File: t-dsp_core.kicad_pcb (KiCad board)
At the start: 4 copper layers, 100 x 61 mm, 160 parts, among them IC1 Logic Level Shifter - 74HCT2G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, J1 J_PWR, J10 J_DMX, J11 J_LED, J12 J_ETH, J13 u.FL DNP (IDC767 ext-antenna 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, J2 J_TDM, J3 J_T, J4 J_USBH, J5 J_MIDI, J6 J_SPDIF, J7 J_AUX, J8 J_S3, T108 Tab, T109 Tab, T110 Tab, T111 Tab, U1 Teensy 4.1 - DEVKIT, U11 Dual Buffer - SN74LVC2G125DCTR, U13 ESP32-S3-WROOM-1-N16R8, U15 LT3045EMSE#TRPBF, U16 THVD1450DR, U17 ISO7762DW, U18 TEA1-0505HI, U19 SRC4382IPFBR, U20 TLV75718PDRVR, U21 74LVC157APW, U22 IDC777-1, U23 74LVC157APW, U24 AP63203WU, U3 Power Mux & Protect - TPS2116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, U4 Optoisolators - H11L1SM - 6-S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, U5 SN74LVC541APWR, U9 Dual Buffer - 74HCT2G17GW,125, Y1 24.576MHz

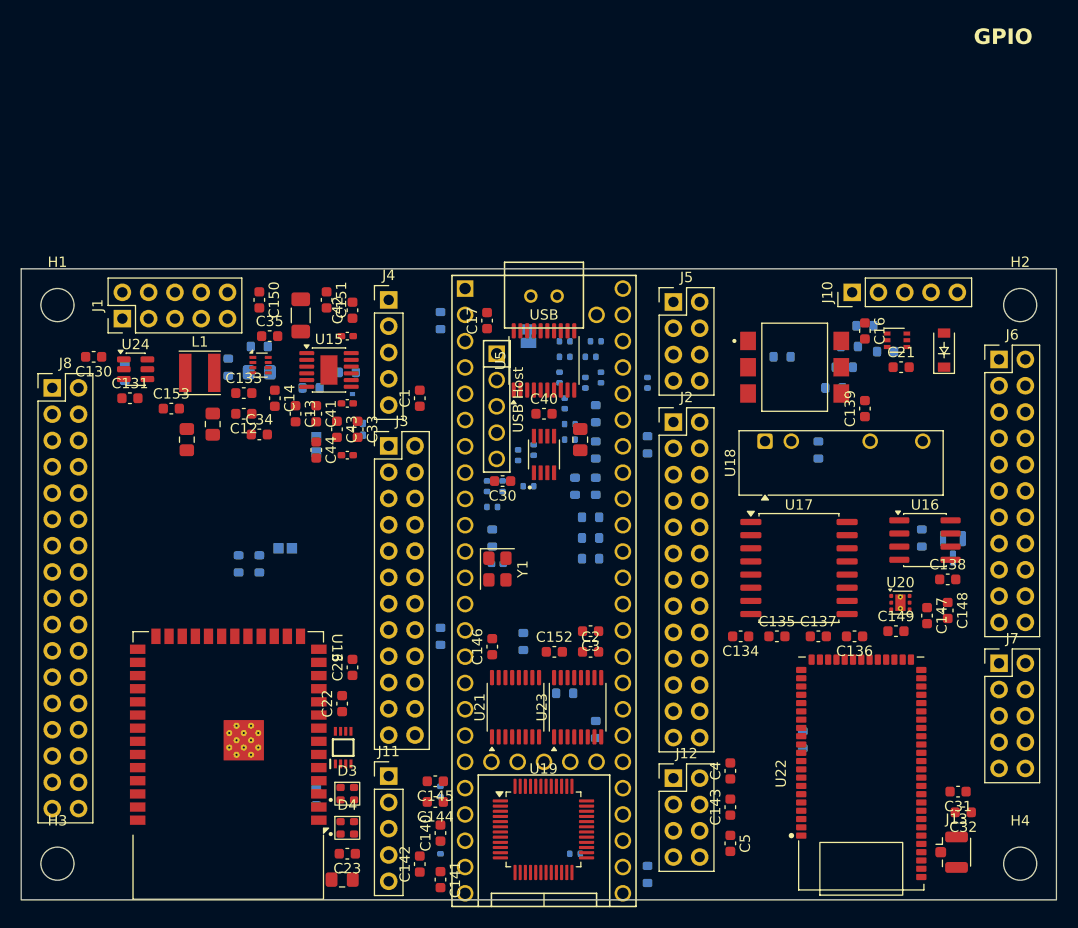
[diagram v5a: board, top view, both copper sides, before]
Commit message: Spin 2 stage 10v (board): J2 2x14, U6/U7 in the buffer column under the Teensy, 3 series R + 8 jumpers + 2 caps added and placed (back side), two stray track fragments from the old design removed; synced with pcbnew, parity clean
Co-Authored-By: Claude Fable 5.1 <noreply@anthropic.com>
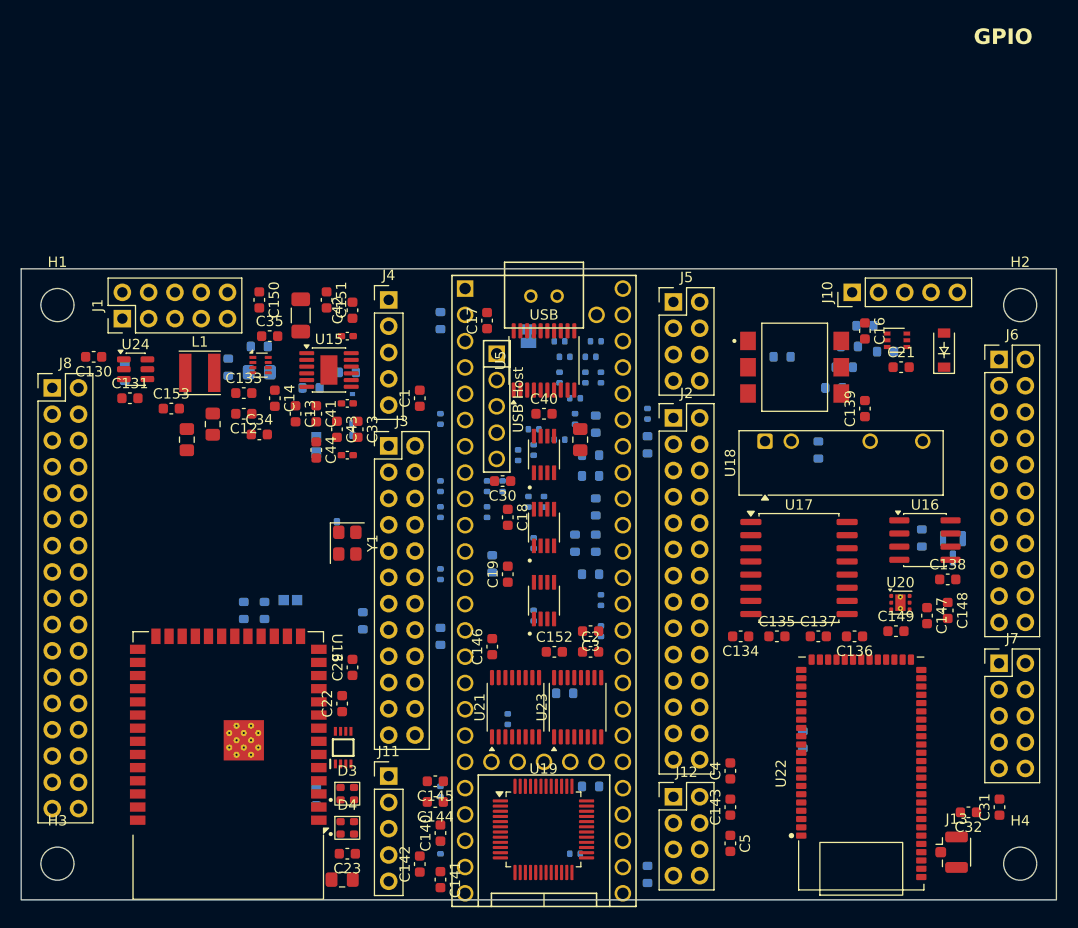
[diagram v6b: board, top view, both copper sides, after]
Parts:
- added C18: 100nF, Capacitor_SMD:C_0603_1608Metric, F.Cu at (147.0, 163.0)
- added C19: 100nF, Capacitor_SMD:C_0603_1608Metric, F.Cu at (147.0, 168.5)
- added R75: 33 ohm, Resistor_SMD:R_0402_1005Metric, B.Cu at (156.0, 174.0)
- added R76: 33 ohm, Resistor_SMD:R_0402_1005Metric, B.Cu at (147.0, 182.5)
- added R77: 0 ohm, Resistor_SMD:R_0402_1005Metric, B.Cu at (149.5, 165.5)
- added R78: 0 ohm DNP, Resistor_SMD:R_0402_1005Metric, B.Cu at (140.5, 162.5)
- added R79: 0 ohm DNP, Resistor_SMD:R_0402_1005Metric, B.Cu at (149.0, 161.5)
- added R80: 0 ohm, Resistor_SMD:R_0402_1005Metric, B.Cu at (140.5, 160.0)
- added R81: 33 ohm, Resistor_SMD:R_0402_1005Metric, B.Cu at (156.0, 171.0)
- added R82: 0 ohm DNP, Resistor_SMD:R_0402_1005Metric, B.Cu at (149.5, 172.5)
- added R83: 0 ohm, Resistor_SMD:R_0402_1005Metric, B.Cu at (140.5, 168.5)
- added R84: 0 ohm, Resistor_SMD:R_0402_1005Metric, B.Cu at (149.5, 154.5)
- added R85: 0 ohm DNP, Resistor_SMD:R_0402_1005Metric, B.Cu at (140.5, 153.5)
- added U6: SN74LVC2G125DCTR, project_fp:SOP65P400X130-8N, F.Cu at (150.5, 164.0)
- added U7: SN74LVC2G125DCTR, project_fp:SOP65P400X130-8N, F.Cu at (150.5, 171.1)
- J2: footprint Connector_PinHeader_2.54mm:PinHeader_2x13_P2.54mm_Vertical -> Connector_PinHeader_2.54mm:PinHeader_2x14_P2.54mm_Vertical
- moved R60 15.9 mm to (130.5, 164.0), turned to 90 degrees
- moved R61 15.6 mm to (133.0, 173.0)
- moved Y1 14.7 mm to (131.5, 165.5)
- moved R47 7.83 mm to (153.5, 153.5)
- moved R6 7.57 mm to (160.5, 153.0), turned to 90 degrees
- moved R11 5.52 mm to (155.0, 189.0), turned to 0 degrees
- moved R12 5.50 mm to (155.5, 162.0), turned to -90 degrees
- moved PU_EN1 5.02 mm to (126.0, 171.0)
- moved R67 4.53 mm to (123.5, 172.0)
- moved R68 4.53 mm to (121.5, 172.0)
- moved C31 4.27 mm to (194.5, 191.0), turned to 90 degrees
- moved R14 3.35 mm to (155.0, 157.0), turned to 180 degrees
- moved R15 2.55 mm to (155.5, 165.5), turned to 90 degrees
- moved R19 2.50 mm to (145.5, 167.5)
- moved R56 2.12 mm to (150.5, 161.5), turned to -90 degrees
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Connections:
- net Net-(U1-32_OUT1B) renamed /OUT1B_MCU
- U11 pad 7: GND -> /OUT1C_OE_IN

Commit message: Spin 2 stage 10w: LED driver IC1 and D3/D4 to the middle of the left column; passives re-placed
Co-Authored-By: Claude Fable 5.1 <noreply@anthropic.com>
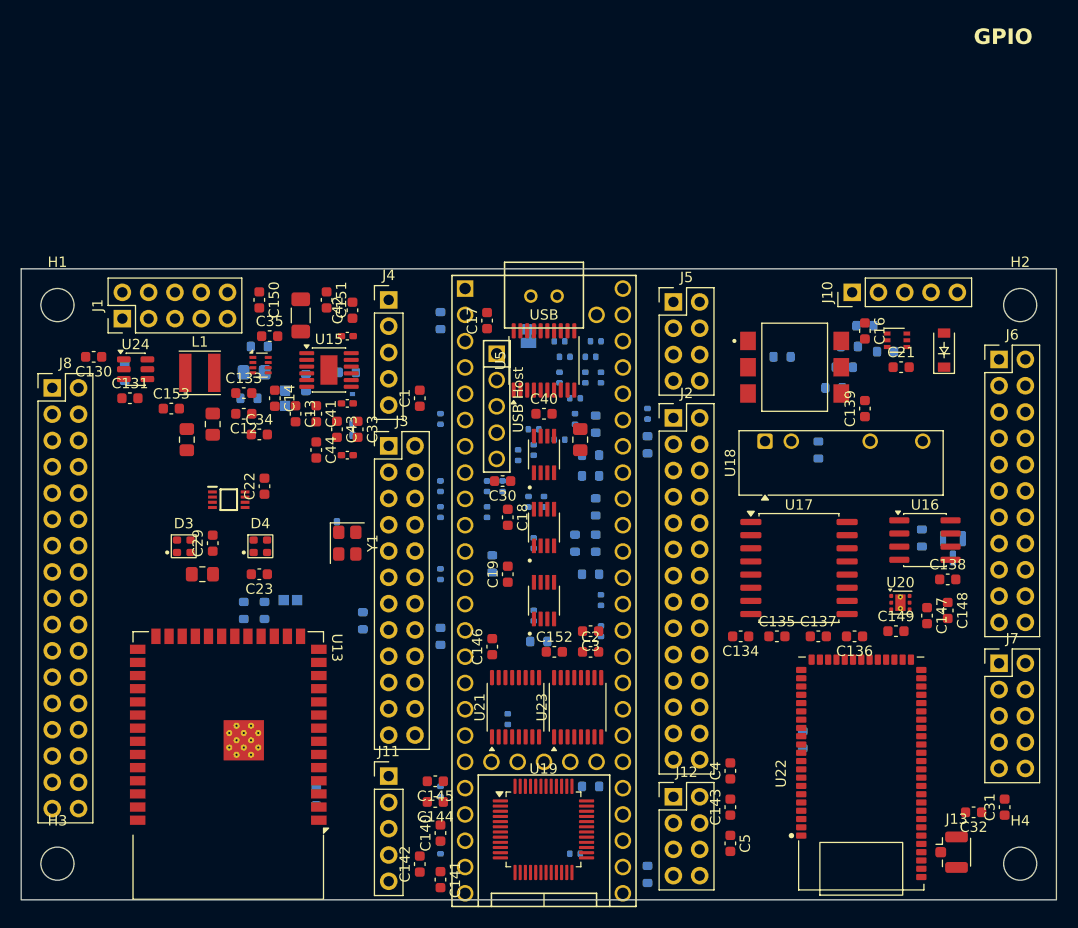
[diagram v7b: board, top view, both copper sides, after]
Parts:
- moved C28 32.4 mm to (117.5, 168.5), turned to 0 degrees
- moved D3 28.7 mm to (115.7, 165.8)
- moved D4 28.5 mm to (123.1, 165.8)
- moved C23 28.3 mm to (123.0, 168.5)
- moved IC1 26.4 mm to (120.0, 161.3), turned to 0 degrees
- moved C22 22.3 mm to (123.5, 160.0)
- moved C29 18.1 mm to (118.5, 165.5)
- moved R8 5.59 mm to (150.0, 175.0)
- moved FL1 5.41 mm to (125.5, 151.5)
- moved R29 3.61 mm to (122.0, 151.5), turned to 0 degrees
- moved R58 0.71 mm to (127.5, 150.0), turned to -90 degrees
- moved C31 0.50 mm to (195.0, 191.0)
- moved C32 0.50 mm to (192.0, 191.5)
- moved R28 0.50 mm to (122.5, 149.0)

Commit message: Spin 2 stage 10y (2/2, board): SAI2 block footprints synced and placed; stage 10x power parts placed
- swap_fp/sync_fields from the stage 10y netlist: U19 TSSOP-16 (257), U21 TSSOP-20 (244), U23 TSSOP-16 (138), U20 SOP-8 (2G125), J7 2x6 J_SAI2, J4 2x5 J_USB, D7 SMA + Q1 SOT-23 added; J6, U3, C13/C14, R28-R30, C144-C149, C152, R1/R2/R10 removed; R86-R101 added.
- Placement: U19/U23 under the Teensy (slot 2, Y 38.5), U21 and U20 in the right column beside J_SAI2, D7/Q1 in the power row where the TPS2116 was; passives re-placed two-sided by the net-driven placer (131 parts, median 2.4 mm / mean 3.4 mm to their pin).
- Three leftover /OUT1B_MCU track fragments from the old design removed; the board has no routing.
- DRC with schematic parity: only the pre-existing U13 courtyard (antenna keep-out) vs H3/J11, the U13 0.2 mm thermal-via holes and the board_outline2 outline footprint remain.

Co-Authored-By: Claude Fable 5.1 <noreply@anthropic.com>
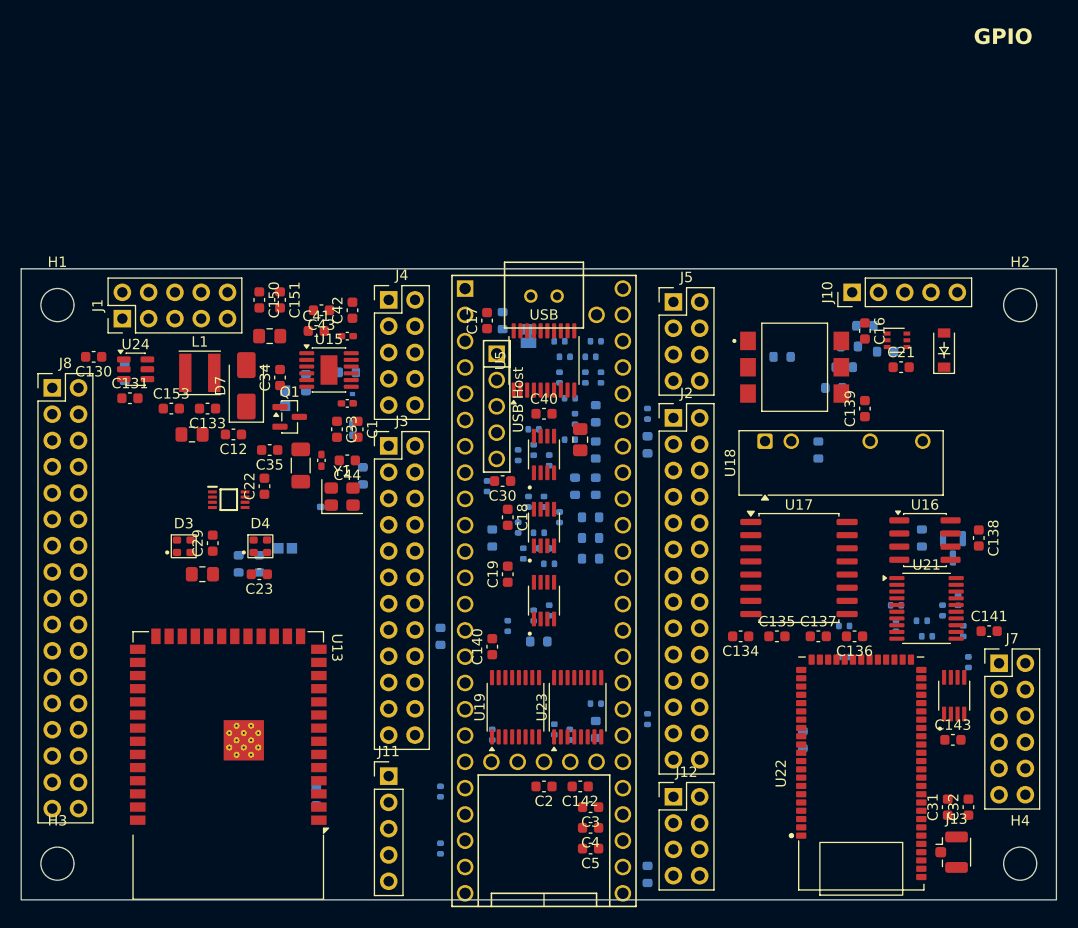
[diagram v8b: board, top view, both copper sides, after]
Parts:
- removed C13: 10 uF, Capacitor_SMD:C_0603_1608Metric
- removed C14: 0.1 uF, Capacitor_SMD:C_0603_1608Metric
- removed C144, C145, C148: 10uF, Capacitor_SMD:C_0603_1608Metric
- removed C146, C149, C152: 100nF, Capacitor_SMD:C_0603_1608Metric
- removed C147: 1uF, Capacitor_SMD:C_0603_1608Metric
- removed J6: J_SPDIF, Connector_PinHeader_2.54mm:PinHeader_2x11_P2.54mm_Vertical
- removed R1, R10, R2: 33 ohm, Resistor_SMD:R_0402_1005Metric
- removed R28: 16.9k ohm, project_fp:R_0805_2012Metric_Pad1.15x1.40mm_HandSolder
- removed R29, R30: 5.1k ohm, Resistor_SMD:R_0603_1608Metric
- removed U3: Power Mux & Protect - TPS2116DRL, project_fp:TPS2116DRL
- added D7: SMAJ5.0A, Diode_SMD:D_SMA, F.Cu at (121.8, 150.3)
- added Q1: AO3401A, Package_TO_SOT_SMD:SOT-23, F.Cu at (125.9, 153.3)
- added R100: 33 ohm, Resistor_SMD:R_0402_1005Metric, B.Cu at (179.5, 176.5)
- added R101: 33 ohm, Resistor_SMD:R_0402_1005Metric, B.Cu at (191.0, 174.0)
- added R86: 10k, Resistor_SMD:R_0402_1005Metric, B.Cu at (151.5, 183.5)
- added R87: 10k, Resistor_SMD:R_0402_1005Metric, B.Cu at (153.0, 184.0)
- added R88: 10k, Resistor_SMD:R_0402_1005Metric, B.Cu at (145.5, 184.0)
- added R89: 33 ohm, Resistor_SMD:R_0402_1005Metric, B.Cu at (155.5, 181.0)
- added R90: 33 ohm, Resistor_SMD:R_0402_1005Metric, B.Cu at (160.5, 182.5)
- added R91: 33 ohm, Resistor_SMD:R_0402_1005Metric, B.Cu at (147.0, 173.5)
- added R92: 33 ohm, Resistor_SMD:R_0402_1005Metric, B.Cu at (190.5, 171.0)
- added R93: 33 ohm, Resistor_SMD:R_0402_1005Metric, B.Cu at (189.0, 172.0)
- added R94: 33 ohm, Resistor_SMD:R_0402_1005Metric, B.Cu at (191.5, 177.0)
- added R95: 33 ohm, Resistor_SMD:R_0402_1005Metric, B.Cu at (184.5, 173.5)
- added R96: 33 ohm, Resistor_SMD:R_0402_1005Metric, B.Cu at (184.5, 171.5)
- added R97: 33 ohm, Resistor_SMD:R_0402_1005Metric, B.Cu at (187.0, 173.0)
- added R98: 33 ohm, Resistor_SMD:R_0402_1005Metric, B.Cu at (187.5, 174.5)
- added R99: 33 ohm, Resistor_SMD:R_0402_1005Metric, B.Cu at (179.5, 173.5)
- J4: value J_USBH -> J_USB; footprint Connector_PinHeader_2.54mm:PinHeader_1x05_P2.54mm_Vertical -> Connector_PinHeader_2.54mm:PinHeader_2x05_P2.54mm_Vertical
- J7: value J_AUX -> J_SAI2; footprint Connector_PinHeader_2.54mm:PinHeader_2x05_P2.54mm_Vertical -> Connector_PinHeader_2.54mm:PinHeader_2x06_P2.54mm_Vertical
- U19: value SRC4382IPFBR -> SN74LVC257APWR; footprint Package_QFP:TQFP-48_7x7mm_P0.5mm -> Package_SO:TSSOP-16_4.4x5mm_P0.65mm
- U20: value TLV75718PDRVR -> SN74LVC2G125DCTR; footprint Package_SON:WSON-6-1EP_2x2mm_P0.65mm_EP1x1.6mm_ThermalVias -> project_fp:SOP65P400X130-8N
- U21: value 74LVC157APW -> SN74LVC244APWR; footprint Package_SO:TSSOP-16_4.4x5mm_P0.65mm -> Package_SO:TSSOP-20_4.4x6.5mm_P0.65mm
- U23: value 74LVC157APW -> SN74LVC138APWR
- moved C141 58.2 mm to (193.5, 174.0), turned to 0 degrees
- moved U21 40.8 mm to (187.4, 171.8), turned to 0 degrees
- moved C143 22.5 mm to (190.0, 184.5), turned to 0 degrees
- moved C140 18.7 mm to (145.5, 175.5)
- moved C142 17.2 mm to (154.0, 189.0), turned to 180 degrees
- moved C3 17.0 mm to (155.0, 191.0)
- moved R76 16.9 mm to (150.5, 166.0), turned to 180 degrees
- moved C4 14.6 mm to (155.0, 193.0), turned to 180 degrees
- moved C15 14.5 mm to (127.0, 158.0), turned to -90 degrees
- moved R61 14.0 mm to (133.0, 159.0), turned to 90 degrees
- moved C2 13.8 mm to (150.5, 189.0), turned to 180 degrees
- moved C5 13.5 mm to (155.0, 195.0), turned to 180 degrees
- moved U19 12.1 mm to (147.8, 181.4), turned to 90 degrees
- moved R75 11.7 mm to (152.0, 163.0)
- moved C43 11.6 mm to (129.0, 143.0), turned to 180 degrees
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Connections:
- C141 pad 1: +1V8 -> 3.3V_DIG
- J3 pad 17: T22 -> GND
- J3 pad 18: T26 -> GND
- J3 pad 19: T27 -> GND
- J3 pad 22: /T33_MCLK2 -> GND
- J4 pad 2: HOST_D1- -> GND
- J4 pad 3: HOST_D1+ -> HOST_D1-
- J4 pad 4: GND -> T_USB_DN
- J4 pad 5: HOST_5V -> HOST_D1+
- J7 pad 10: GND -> AUX_I2S_DOUT
- J7 pad 3: AUX_I2S_BCK -> AUX_I2S_MCLK
- J7 pad 5: GND -> AUX_I2S_BCK
- J7 pad 6: AUX_I2S_LRCK -> GND
- J7 pad 7: AUX_I2S_DIN -> AUX_I2S_LRCK
- J7 pad 8: AUX_I2S_OUT -> GND
- J7 pad 9: GND -> AUX_I2S_DIN
- J8 pad 25: S3_IO40 -> GND
- J8 pad 26: S3_IO41 -> GND
- U1 pad 18: T26 -> SAI2_MODE0
- U1 pad 19: T27 -> SAI2_MODE1
- U1 pad 25: Net-(U1-33_MCLK2) -> SAI2_MCLK
- U1 pad 4: 2_OUT2 -> SAI2_OUT
- U1 pad 44: T22 -> SAI2_SEL
- U1 pad 49: 5V_VUSB -> unconnected-(U1-VUSB-Pad49)
- U1 pad 5: Net-(U1-3_LRCLK2) -> SAI2_LRCLK
- U1 pad 6: Net-(U1-4_BCLK2) -> SAI2_BCLK
- U1 pad 66: unconnected-(U1-D--Pad66) -> T_USB_DN
- U1 pad 67: unconnected-(U1-D+-Pad67) -> T_USB_DP
- U1 pad 7: 5_IN2 -> SAI2_IN
- U13 pad 33: S3_IO40 -> BT_RST
- U13 pad 34: S3_IO41 -> BT_SYS_CTRL
- U19 pad 1: SPDIF_RX1P -> SAI2_SEL
- U19 pad 11: unconnected-(U19-~LOCK-Pad11) -> GND
- U19 pad 12: unconnected-(U19-RXCKO-Pad12) -> Net-(U19-Zc)
- U19 pad 13: unconnected-(U19-RXCKI-Pad13) -> S3_I2S_DOUT
- U19 pad 14: GND -> BT_SDATA
- U19 pad 15: unconnected-(U19-~RDY-Pad15) -> SAI2_nOE_INT
- U19 pad 16: GND -> 3.3V_DIG
- U19 pad 2: SPDIF_RX1N -> BT_BCK
- U19 pad 3: SPDIF_RX2P -> S3_I2S_BCK
- U19 pad 4: SPDIF_RX2N -> Net-(U19-Za)
- U19 pad 5: SPDIF_RX3P -> BT_LRCK
- U19 pad 6: SPDIF_RX3N -> S3_I2S_LRCK
- U19 pad 7: SPDIF_RX4P -> Net-(U19-Zb)
- U19 pad 8: SPDIF_RX4N -> GND
- U19 pad 9: 3.3V_DIG -> unconnected-(U19-Zd-Pad9)
- U20 pad 1: +1V8 -> SAI2_nOE_HDR
- U20 pad 2: +1V8 -> AUX_I2S_DIN
- U20 pad 3: GND -> Net-(U20-2Y)
- U20 pad 4: 3.3V_DIG -> GND
- U20 pad 5: GND -> AUX_I2S_DIN
- U20 pad 6: 3.3V_DIG -> Net-(U20-1Y)
- U20 pad 7: GND -> SAI2_nOE_OUT
- U21 pad 1: BT_S3_SEL -> SAI2_nOE_HDR
- U21 pad 11: GND -> SAI2_BCLK
- U21 pad 12: MUX1_SDATA -> Net-(U21-O3a)
- U21 pad 13: S3_I2S_DOUT -> SAI2_LRCLK
- U21 pad 14: BT_SDATA -> Net-(U21-O2a)
- U21 pad 15: GND -> SAI2_MCLK
- U21 pad 16: 3.3V_DIG -> Net-(U21-O1a)
- U21 pad 2: BT_BCK -> AUX_I2S_BCK
- U21 pad 3: S3_I2S_BCK -> Net-(U21-O3b)
- U21 pad 4: MUX1_BCK -> AUX_I2S_LRCK
- U21 pad 5: BT_LRCK -> Net-(U21-O2b)
- U21 pad 6: S3_I2S_LRCK -> SAI2_MCLK
- U21 pad 7: MUX1_LRCK -> Net-(U21-O1b)
- U21 pad 8: GND -> SAI2_OUT
- U21 pad 9: unconnected-(U21-Zc-Pad9) -> Net-(U21-O0b)
- U23 pad 1: AUX_SEL -> SAI2_MODE0
- U23 pad 10: GND -> unconnected-(U23-O5-Pad10)
- U23 pad 11: GND -> unconnected-(U23-O4-Pad11)
- U23 pad 12: SRC_A_SDATA -> unconnected-(U23-O3-Pad12)
- U23 pad 13: AUX_I2S_DIN -> SAI2_nOE_OUT
- U23 pad 14: MUX1_SDATA -> SAI2_nOE_HDR
- U23 pad 15: GND -> SAI2_nOE_INT
- U23 pad 2: MUX1_BCK -> SAI2_MODE1
- U23 pad 3: AUX_I2S_BCK -> GND
- U23 pad 4: SRC_A_BCK -> GND
- U23 pad 5: MUX1_LRCK -> GND
- U23 pad 6: AUX_I2S_LRCK -> 3.3V_DIG
- U23 pad 7: SRC_A_LRCK -> unconnected-(U23-O7-Pad7)
